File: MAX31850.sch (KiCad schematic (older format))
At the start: 8 parts, among them J1 K Type, U1 MAX31850KATB

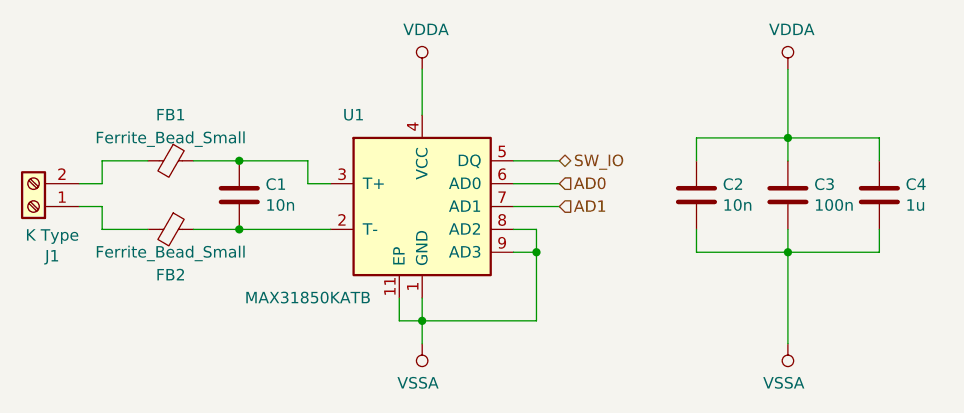
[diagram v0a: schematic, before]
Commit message: Added optional through hole resistor to set fan switch on temperature.
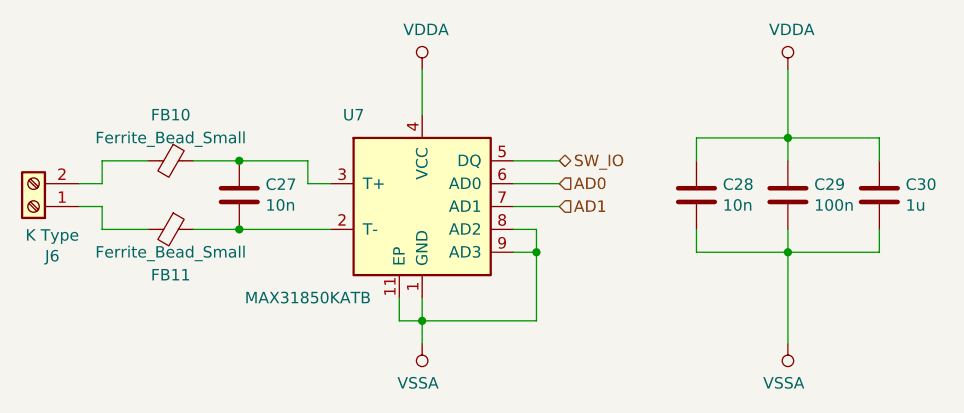
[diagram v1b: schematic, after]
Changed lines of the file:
@@
 AR Path="/5E3E3667/5E3B5F5C" Ref="U6"  Part="1"
 AR Path="/5E3E8E80/5E3B5F5C" Ref="U7"  Part="1"
-F 0 "U1" H 4700 2800 50  0000 C CNN
+F 0 "U7" H 4700 2800 50  0000 C CNN
 F 1 "MAX31850KATB" H 4500 2000 50  0000 C CNN
 F 2 "global:TDFN-10-1EP_3x4mm_Pitch0.5mm" H 5000 2400 50  0001 C CIN
@@
 AR Path="/5E3E3667/5E3B92B5" Ref="#PWR032"  Part="1"
 AR Path="/5E3E8E80/5E3B92B5" Ref="#PWR036"  Part="1"
-F 0 "#PWR08" H 5000 1650 50  0001 C CNN
+F 0 "#PWR036" H 5000 1650 50  0001 C CNN
 F 1 "VDDA" H 5017 1973 50  0000 C CNN
 F 2 "" H 5000 1800 50  0001 C CNN
@@
 AR Path="/5E3E3667/5E3B9C37" Ref="#PWR033"  Part="1"
 AR Path="/5E3E8E80/5E3B9C37" Ref="#PWR037"  Part="1"
-F 0 "#PWR09" H 5000 2850 50  0001 C CNN
+F 0 "#PWR037" H 5000 2850 50  0001 C CNN
 F 1 "VSSA" H 5018 3173 50  0000 C CNN
 F 2 "" H 5000 3000 50  0001 C CNN
@@
 AR Path="/5E3E3667/5E3C171C" Ref="C23"  Part="1"
 AR Path="/5E3E8E80/5E3C171C" Ref="C27"  Part="1"
-F 0 "C1" H 4315 2396 50  0000 L CNN
+F 0 "C27" H 4315 2396 50  0000 L CNN
 F 1 "10n" H 4315 2305 50  0000 L CNN
 F 2 "Capacitor_SMD:C_0603_1608Metric" H 4238 2200 50  0001 C CNN
@@
 AR Path="/5E3E3667/5E3C59DE" Ref="FB8"  Part="1"
 AR Path="/5E3E8E80/5E3C59DE" Ref="FB10"  Part="1"
-F 0 "FB1" V 3700 2200 50  0000 C CNN
+F 0 "FB10" V 3700 2200 50  0000 C CNN
 F 1 "Ferrite_Bead_Small" V 3800 2200 50  0000 C CNN
 F 2 "Inductor_SMD:L_0603_1608Metric" V 3830 2200 50  0001 C CNN
@@
 AR Path="/5E3E3667/5E3C8A66" Ref="FB9"  Part="1"
 AR Path="/5E3E8E80/5E3C8A66" Ref="FB11"  Part="1"
-F 0 "FB2" V 4100 2500 50  0000 C CNN
+F 0 "FB11" V 4100 2500 50  0000 C CNN
 F 1 "Ferrite_Bead_Small" V 4000 2500 50  0000 C CNN
 F 2 "Inductor_SMD:L_0603_1608Metric" V 3830 2500 50  0001 C CNN
@@
 AR Path="/5E3E3667/5E3CBB76" Ref="J5"  Part="1"
 AR Path="/5E3E8E80/5E3CBB76" Ref="J6"  Part="1"
-F 0 "J1" H 3218 2617 50  0000 C CNN
+F 0 "J6" H 3218 2617 50  0000 C CNN
 F 1 "K Type" H 3218 2526 50  0000 C CNN
 F 2 "Connector_Phoenix_MC:PhoenixContact_MC_1,5_2-G-3.81_1x02_P3.81mm_Horizontal" H 3300 2400 50  0001 C CNN
@@
 AR Path="/5E3E3667/5E3D0C8B" Ref="C25"  Part="1"
 AR Path="/5E3E8E80/5E3D0C8B" Ref="C29"  Part="1"
-F 0 "C3" H 6715 2396 50  0000 L CNN
+F 0 "C29" H 6715 2396 50  0000 L CNN
 F 1 "100n" H 6715 2305 50  0000 L CNN
 F 2 "Capacitor_SMD:C_0603_1608Metric" H 6638 2200 50  0001 C CNN
@@
 AR Path="/5E3E3667/5E3DBF02" Ref="C26"  Part="1"
 AR Path="/5E3E8E80/5E3DBF02" Ref="C30"  Part="1"
-F 0 "C4" H 7115 2396 50  0000 L CNN
+F 0 "C30" H 7115 2396 50  0000 L CNN
 F 1 "1u" H 7115 2305 50  0000 L CNN
 F 2 "Capacitor_SMD:C_0805_2012Metric" H 7038 2200 50  0001 C CNN
@@
 AR Path="/5E3E3667/5E3DE9FD" Ref="#PWR034"  Part="1"
 AR Path="/5E3E8E80/5E3DE9FD" Ref="#PWR038"  Part="1"
-F 0 "#PWR010" H 6600 1650 50  0001 C CNN
+F 0 "#PWR038" H 6600 1650 50  0001 C CNN
 F 1 "VDDA" H 6617 1973 50  0000 C CNN
 F 2 "" H 6600 1800 50  0001 C CNN
@@
 AR Path="/5E3E3667/5E3DFF6B" Ref="#PWR035"  Part="1"
 AR Path="/5E3E8E80/5E3DFF6B" Ref="#PWR039"  Part="1"
-F 0 "#PWR011" H 6600 2850 50  0001 C CNN
+F 0 "#PWR039" H 6600 2850 50  0001 C CNN
 F 1 "VSSA" H 6618 3173 50  0000 C CNN
 F 2 "" H 6600 3000 50  0001 C CNN
@@
 AR Path="/5E3E3667/5E3F83EC" Ref="C24"  Part="1"
 AR Path="/5E3E8E80/5E3F83EC" Ref="C28"  Part="1"
-F 0 "C2" H 6315 2396 50  0000 L CNN
+F 0 "C28" H 6315 2396 50  0000 L CNN
 F 1 "10n" H 6315 2305 50  0000 L CNN
 F 2 "Capacitor_SMD:C_0603_1608Metric" H 6238 2200 50  0001 C CNN
